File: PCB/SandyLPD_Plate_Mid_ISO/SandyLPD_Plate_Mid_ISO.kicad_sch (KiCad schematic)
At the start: 4 parts, among them SW1 SW_Push, SW2 SW_Push

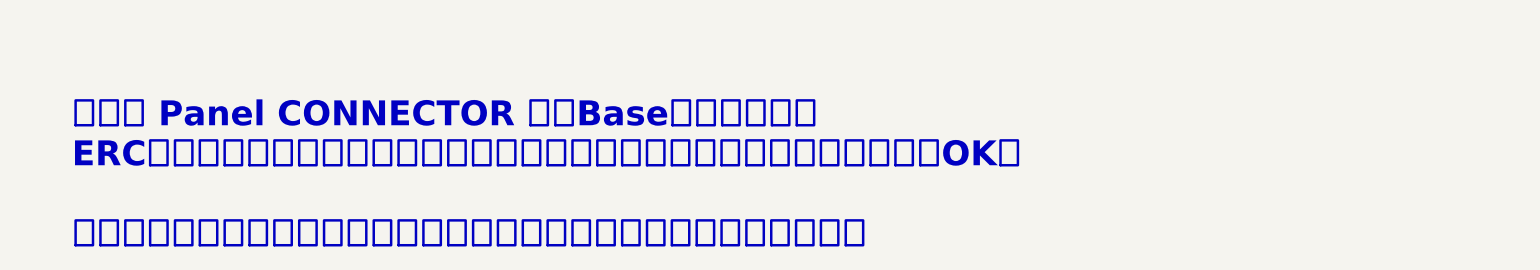
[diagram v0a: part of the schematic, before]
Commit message: 不要コメント削除
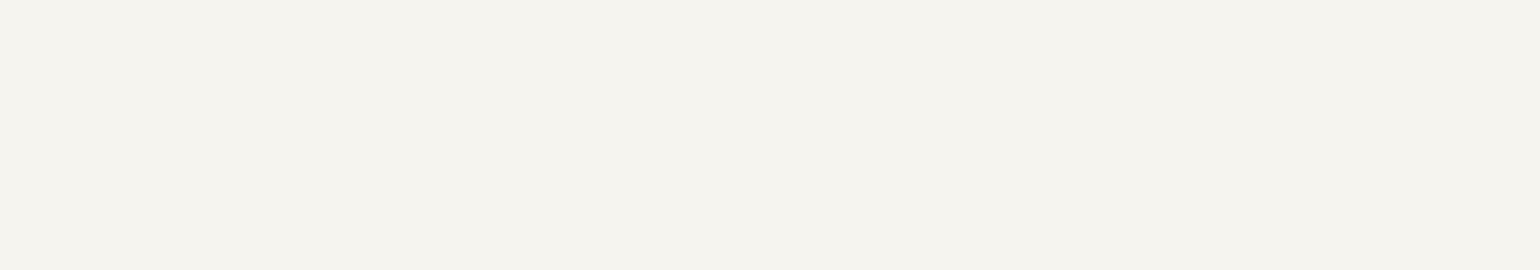
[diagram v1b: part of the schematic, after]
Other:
- note removed: "以下の Panel CONNECTOR は、Baseからコピペ。 ERCの警告「別パネルのラベルがどこにも接続されていない」は、無視してOK。 ！！！他の警告（ラベルかぶりとか）は、しっかりチェックせよ！！！"
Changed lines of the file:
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@@
 		(at 69.215 88.9)
-	)
-	(text "以下の Panel CONNECTOR は、Baseからコピペ。\nERCの警告「別パネルのラベルがどこにも接続されていない」は、無視してOK。\n\n！！！他の警告（ラベルかぶりとか）は、しっかりチェックせよ！！！"
-		(exclude_from_sim no)
-		(at 26.035 257.81 0)
-		(effects
-			(font
-				(size 5.08 5.08)
-				(thickness 0.508)
-				(bold yes)
-			)
-			(justify left bottom)
-		)
 	)
 	(text "SCREWS to Mid"
